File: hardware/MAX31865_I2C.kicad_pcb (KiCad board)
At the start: 2 copper layers, 25.4 x 27.9 mm, 39 parts, among them J1 Conn_01x08, J2 AVR-ISP-6, J3 Conn_02x04_Odd_Even, J4 Conn_02x04_Odd_Even, J5 Conn_02x02_Odd_Even, U1 ATmega48A-A, Y1 16MHz

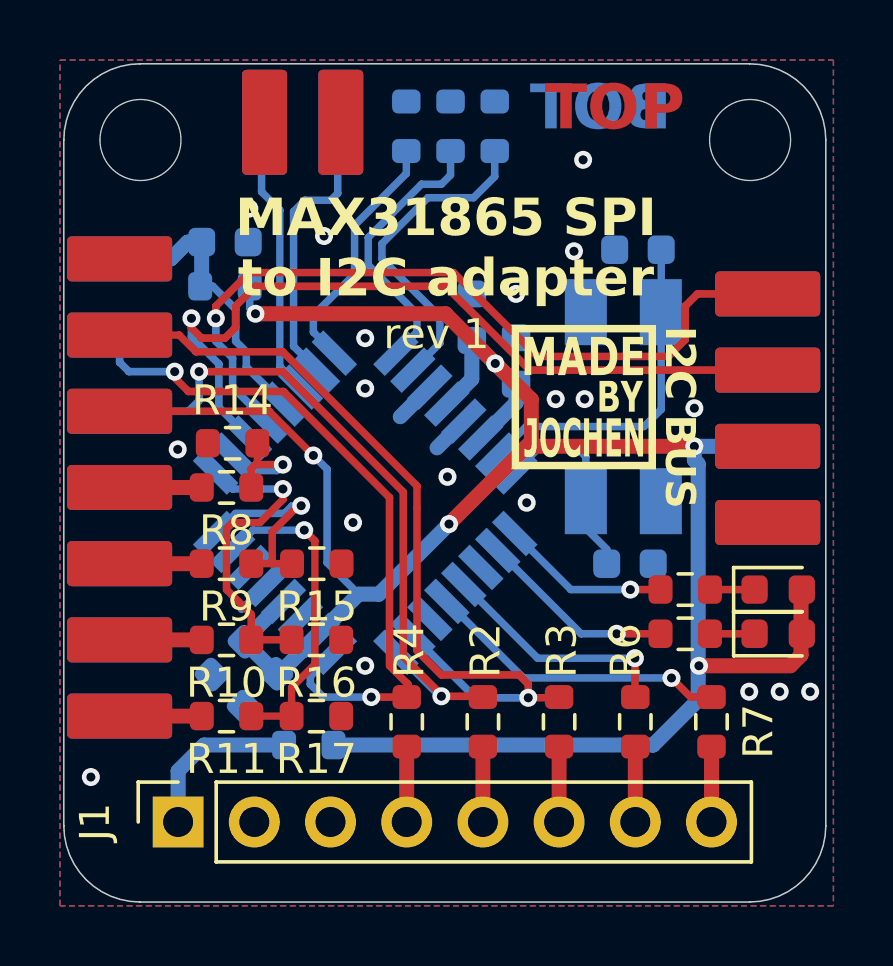
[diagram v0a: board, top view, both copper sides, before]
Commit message: fixed edge connectors for ISP
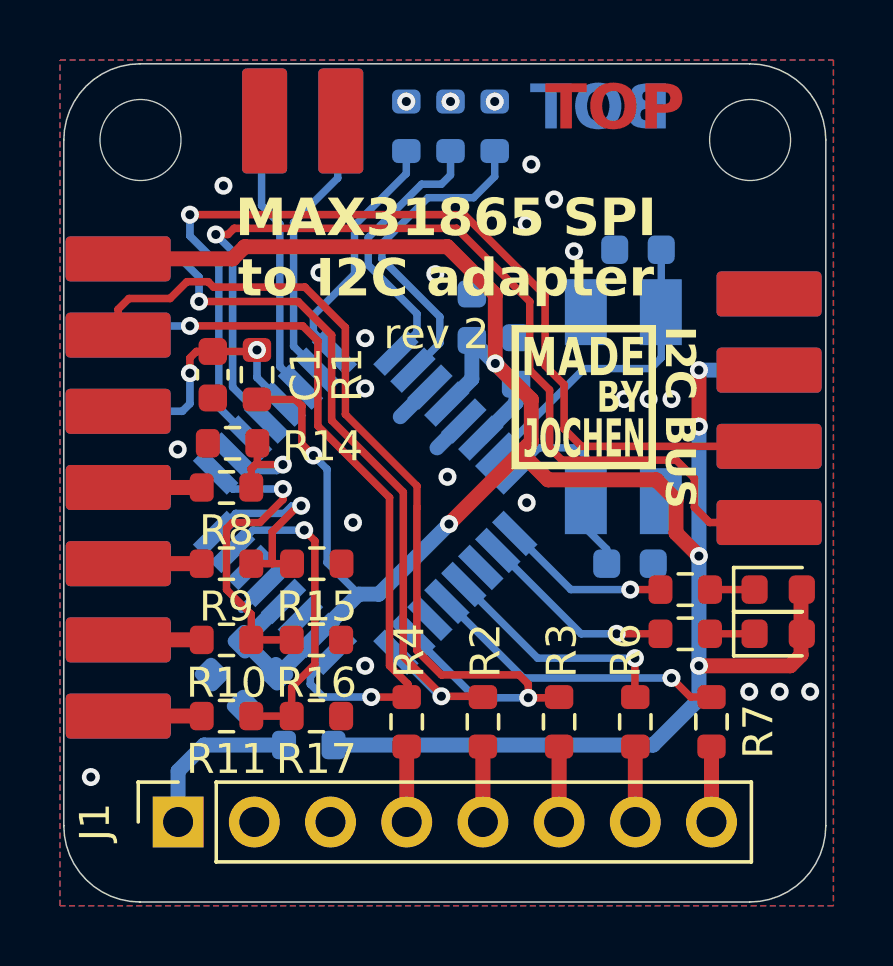
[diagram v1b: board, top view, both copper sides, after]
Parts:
- C1, J2, J3, J5, R1: moved to F.Cu
- J4: moved to B.Cu
- moved C1 4.44 mm to (140.8, 101.4), turned to -90 degrees
- moved R1 3.13 mm to (142.2, 101.4), turned to 90 degrees
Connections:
- J5 pad 1: /RXD -> /TXD
- J5 pad 3: /TXD -> /RXD
- R10 pad 2: Net-(J4-Pin_5) -> Net-(J4-Pin_3)
- R11 pad 2: Net-(J4-Pin_7) -> Net-(J4-Pin_1)
- R8 pad 2: Net-(J4-Pin_1) -> Net-(J4-Pin_7)
- R9 pad 2: Net-(J4-Pin_3) -> Net-(J4-Pin_5)
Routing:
- net +5V: track 81.9 -> 89.1 mm, vias 6 -> 7
- net /SCL: track 26.1 -> 32.5 mm
- net /SDA: track 26.8 -> 33.0 mm
- net /MOSI: track 27.8 -> 31.5 mm
- net /MISO: track 23.0 -> 25.7 mm
- net /SCK: track 23.5 -> 24.8 mm
- net /~{RESET}: track 9.71 -> 8.54 mm, vias 0 -> 2
- net Net-(U1-XTAL1/PB6): track 11.4 -> 10.4 mm
- net /TXD: track 9.73 -> 9.22 mm
- net GND: vias 19 -> 24

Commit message: GPIO input section redesign
Satisfies now the inner Monk
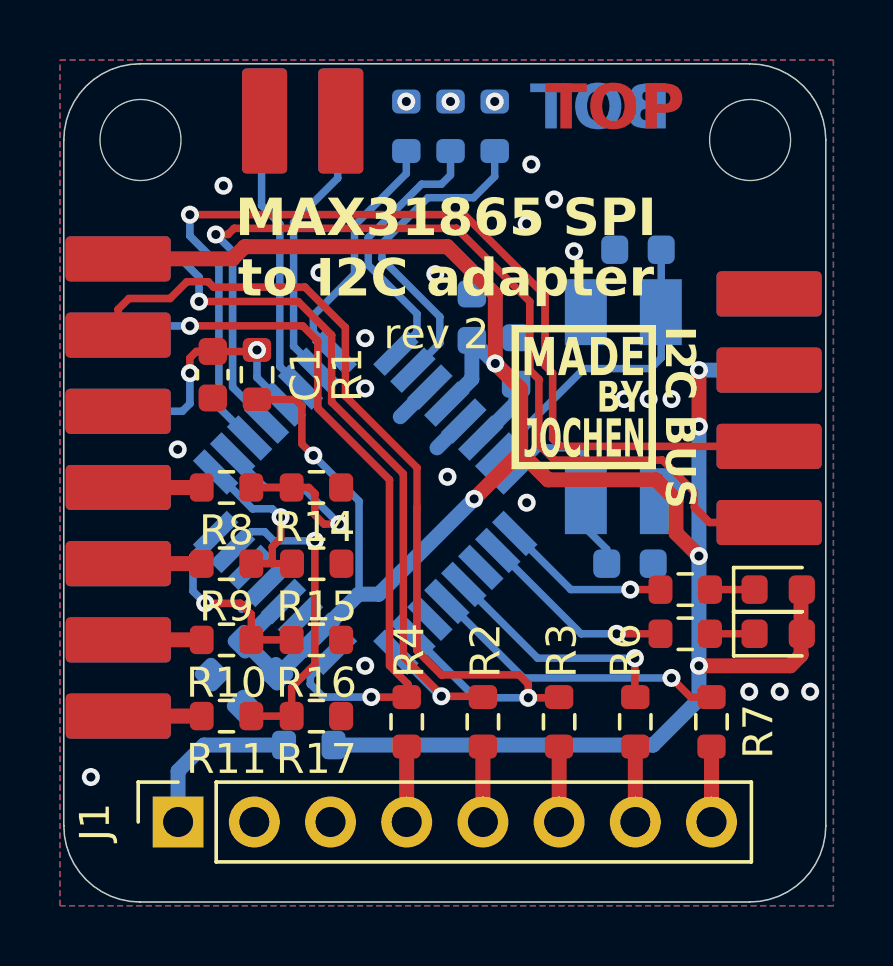
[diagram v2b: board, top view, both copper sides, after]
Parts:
- moved R14 3.16 mm to (144.2, 105.2), turned to 180 degrees
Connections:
- R10 pad 1: /GPIO2 -> /GPIO1
- R15 pad 2: /GPIO1 -> /GPIO2
- R16 pad 2: /GPIO2 -> /GPIO1
- R9 pad 1: /GPIO1 -> /GPIO2
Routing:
- net /GPIO2: track 10.6 -> 5.92 mm
- net /GPIO0: track 4.64 -> 8.37 mm
- net GND: vias 24 -> 23
